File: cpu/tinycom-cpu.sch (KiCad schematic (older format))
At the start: 4 parts, among them P1 CONN_02X08, P2 CONN_02X08, U1 OLIMEX_IC_A13, U2 H5TQG63BFR/FBGA96

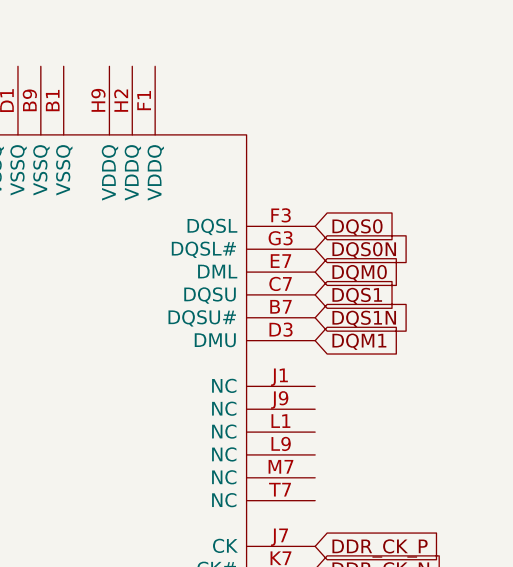
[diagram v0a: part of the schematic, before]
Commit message: add missing ddr connecitons
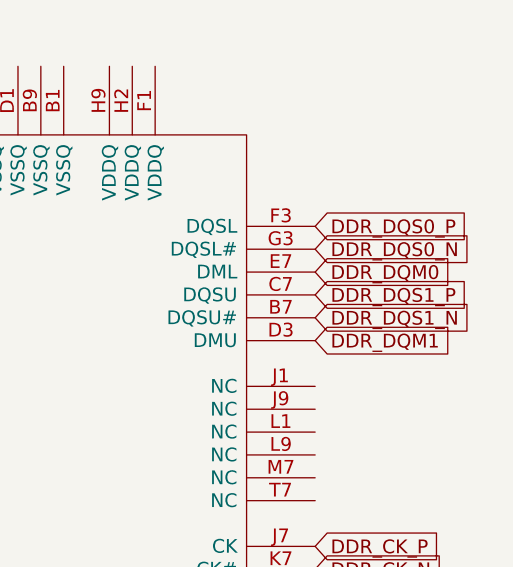
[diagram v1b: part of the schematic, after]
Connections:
- net DQM0 is gone; now on net DDR_DQM0: U2.E7 (DML)
- net DQM1 is gone; now on net DDR_DQM1: U2.D3 (DMU)
- net DQS0 is gone; now on net DDR_DQS0_P: U2.F3 (DQSL)
- net DQS0N is gone; now on net DDR_DQS0_N: U2.G3 (DQSL#)
- net DQS1N is gone; now on net DDR_DQS1_N: U2.B7 (DQSU#)
- net DQS1 renamed DDR_DQS1_P
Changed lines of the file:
@@
 LIBS:sn75lvds83
 LIBS:sy8008baac
-LIBS:cellpilot-cache
+LIBS:tinycom-cpu-cache
 EELAYER 25 0
 EELAYER END
@@
 DDR_CKE
 Text GLabel 10800 -400 2    60   Input ~ 0
-DQS1
+DDR_DQS1_P
 Text GLabel 10800 -300 2    60   Input ~ 0
-DQS1N
+DDR_DQS1_N
 Text GLabel 10800 -700 2    60   Input ~ 0
-DQS0
+DDR_DQS0_P
 Text GLabel 10800 -600 2    60   Input ~ 0
-DQS0N
+DDR_DQS0_N
 Text GLabel 10800 -500 2    60   Input ~ 0
-DQM0
+DDR_DQM0
 Text GLabel 10800 -200 2    60   Input ~ 0
-DQM1
+DDR_DQM1
 Text GLabel 10800 3600 2    60   Input ~ 0
 DDR_ODT

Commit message: add routes
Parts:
- added C1, C2: C_Small, Capacitors_SMD:C_0402, symbol C_Small
- added R? (x3): R, symbol R
- added Y1: Crystal, Crystals:crystal_FA238-TSX3225, symbol Crystal
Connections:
- net +1V5: now reaches U2.A1 (VDDQ)
- net +1V5: now also P1.12 (P12), U1.23 (VCC1_DRAM), U1.30 (VCC2_DRAM), U1.43 (VCC3_DRAM), U1.53 (VCC4_DRAM), U1.62 (VCC5_DRAM), U2.A8 (VDDQ), U2.B2 (VDD), U2.C1 (VDDQ), U2.C9 (VDDQ), U2.D2 (VDDQ), U2.D9 (VDD), U2.E9 (VDDQ), U2.F1 (VDDQ), U2.G7 (VDD), U2.H2 (VDDQ), U2.H9 (VDDQ), U2.K2 (VDD), U2.K8 (VDD), U2.N1 (VDD), U2.N9 (VDD), U2.R1 (VDD), U2.R9 (VDD), R?.1
- net GND: now reaches U2.A9 (VSS)
- net GND: now also P2.10 (P10), P2.12 (P12), P2.14 (P14), P2.16 (P16), U1.159 (RESET_N), U2.B1 (VSSQ), U2.B3 (VSS), U2.B9 (VSSQ), U2.D1 (VSSQ), U2.D8 (VSSQ), U2.E1 (VSS), U2.E2 (VSSQ), U2.E8 (VSSQ), U2.F9 (VSSQ), U2.G1 (VSSQ), U2.G8 (VSS), U2.G9 (VSSQ), U2.J2 (VSS), U2.J8 (VSS), U2.L2 (CS), U2.M1 (VSS), U2.M9 (VSS), U2.P1 (VSS), U2.P9 (VSS), U2.T1 (VSS), U2.T9 (VSS), C1.2, C2.2, R?.2, R?.2
- net at U2.H1 (VREFDQ): now also U2.M8 (VREFCA), R?.1, R?.2
- net at U2.L8 (ZQ): now also R?.1
- net +3V3: now reaches U1.100 (VCC2)
- net +3V3: now also P1.16 (P16), U1.142 (VCC3), U1.163 (VCC4), U1.5 (VCC1), U1.76 (V33_HP), U1.80 (VRP), U1.82 (VRA2), U1.83 (VRA1), U1.97 (V33_USB)
- net SDC0_D1: now reaches U1.107 (PF0/SDC0_D1/JTAG_TMS)
- net SDC0_D1: now also P1.1 (P1)
- net SDC0_D0: now reaches U1.108 (PF1/SDC0_D0/JTAG_TDI)
- net SDC0_D0: now also P1.3 (P3)
- net VCC_14: now reaches U1.109 (VDD4_INT)
- net VCC_14: now also P1.10 (P10), U1.11 (VDD3_CPU), U1.149 (VDD5_INT), U1.156 (VDD5_CPU), U1.16 (VDD4_CPU), U1.164 (VDD6_CPU), U1.169 (VDD7_CPU), U1.173 (VDD8_CPU), U1.35 (VDD1_INT), U1.4 (VDD1_CPU), U1.73 (VDD2_INT), U1.9 (VDD2_CPU), U1.98 (VDD3-INT)
- net SDC0_CLK: now reaches U1.110 (PF2/SDC0_CLK/UART0_TX)
- net SDC0_CLK: now also P1.5 (P5)
- net SDC0_CMD: now reaches U1.111 (PF3/SDC0_CMD/JTAG_TDO)
- net SDC0_CMD: now also P1.7 (P7)
- net SDC0_D3: now reaches U1.112 (PF4/SDC0_D3/UART0_RX)
- net SDC0_D3: now also P1.9 (P9)
- net SDC0_D2: now reaches U1.113 (PF5/SDC0_D2/JTAG_TCK)
- net SDC0_D2: now also P1.11 (P11)
- net CSI_CLK: now reaches U1.114 (PE0/CSI_PCLK/SPI2_CS0/EINT14)
- net CSI_CLK: now also P2.1 (P1)
- net CSI_MCLK: now reaches U1.115 (PE1/CSI_MCLK/SPI2_CLK/EINT15)
- net CSI_MCLK: now also P2.3 (P3)
- net CSI_HSYNC: now reaches U1.116 (PE2/CSI_HSYNC/SPI2_MOSI)
- net CSI_HSYNC: now also P2.5 (P5)
- net CSI_VSYNC: now reaches U1.117 (PE3/CSI_VSYNC/SPI2_MISO)
- net CSI_VSYNC: now also P2.7 (P7)
- net CSI_D0: now reaches U1.118 (PE4/CSI_D0/SDC2_D0)
- net CSI_D0: now also P2.9 (P9)
- net CSI_D1: now reaches U1.119 (PE5/CSI_D1/SDC2_D1)
- net CSI_D1: now also P2.11 (P11)
- net CSI_D2: now reaches U1.120 (PE6/CSI_D2/SDC2_D2)
- net CSI_D2: now also P2.13 (P13)
- net CSI_D3: now reaches U1.121 (PE7/CSI_D3/SDC2_D3)
- net CSI_D3: now also P2.15 (P15)
- net CSI_D4: now reaches U1.122 (PE8/CSI_D4/SDC2_CMD)
- net CSI_D4: now also P2.2 (P2)
- net CSI_D5: now reaches U1.123 (PE9/CSI_D5/SDC2_CLK)
- net CSI_D5: now also P2.4 (P4)
- net CSI_D6: now reaches U1.124 (PE10/CSI_D6/UART1_TX)
- net CSI_D6: now also P2.6 (P6)
- net CSI_D7: now reaches U1.125 (PE11/CSI_D7/UART1_RX)
- net CSI_D7: now also P2.8 (P8)
- net UART1_RX: now reaches U1.151 (PG4/UART1_RX/EINT4)
- net UART1_RX: now also P1.15 (P15)
- net UART1_TX: now reaches U1.152 (PG3/UART1_TX/EINT3)
- net UART1_TX: now also P1.13 (P13)
- net at U1.79 (AGND): now also U1.GND_ (GND)
- net VCC_30: now reaches U1.81 (AVCC)
- net VCC_30: now also P1.14 (P14)
- net at U1.91 (X24MOUT): now also C2.1, Y1.2
- net at U1.92 (X24MIN): now also C1.1, Y1.1
- net UDM0: now reaches U1.93 (UDM0)
- net UDM0: now also P1.2 (P2)
- net UDP0: now reaches U1.94 (UDP0)
- net UDP0: now also P1.4 (P4)
- net UDM1: now reaches U1.95 (UDM1)
- net UDM1: now also P1.6 (P6)
- net UDP1: now reaches U1.96 (UDP1)
- net UDP1: now also P1.8 (P8)
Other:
- moved on the sheet: P2

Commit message: add routes
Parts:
- C1, C2: footprint Capacitors_SMD:C_0402 -> Capacitors_SMD:C_0603
- R1, R2, R3: renamed from R?; footprint (none) -> Resistors_SMD:R_0603
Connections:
- net GND: no longer P2.10 (P10)
- net MICIN1: now reaches U1.84 (MICIN1)
- net MICIN1: now also P2.10 (P10)
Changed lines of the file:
@@
 GND
 Text GLabel 9400 5800 2    60   Input ~ 0
-GND
+MICIN1
 Text GLabel 1550 -1650 0    60   Input ~ 0
 VCC_33
@@
 F 0 "C1" H 810 1920 50  0000 L CNN
 F 1 "C_Small" H 810 1770 50  0000 L CNN
-F 2 "Capacitors_SMD:C_0402" H 800 1850 60  0001 C CNN
+F 2 "Capacitors_SMD:C_0603" H 800 1850 60  0001 C CNN
 F 3 "" H 800 1850 60  0000 C CNN
 	1    800  1850
@@
 F 0 "C2" H 810 2220 50  0000 L CNN
 F 1 "C_Small" H 810 2070 50  0000 L CNN
-F 2 "Capacitors_SMD:C_0402" H 800 2150 60  0001 C CNN
+F 2 "Capacitors_SMD:C_0603" H 800 2150 60  0001 C CNN
 F 3 "" H 800 2150 60  0000 C CNN
 	1    800  2150
@@
 $EndComp
 $Comp
-L GND #PWR?
+L GND #PWR06
 U 1 1 5624D2FA
 P 8100 2900
-F 0 "#PWR?" H 8100 2650 50  0001 C CNN
+F 0 "#PWR06" H 8100 2650 50  0001 C CNN
 F 1 "GND" H 8100 2750 50  0000 C CNN
 F 2 "" H 8100 2900 60  0000 C CNN
@@
 $EndComp
 $Comp
-L GND #PWR?
+L GND #PWR07
 U 1 1 5624DA0C
 P 8750 -1400
-F 0 "#PWR?" H 8750 -1650 50  0001 C CNN
+F 0 "#PWR07" H 8750 -1650 50  0001 C CNN
 F 1 "GND" H 8750 -1550 50  0000 C CNN
 F 2 "" H 8750 -1400 60  0000 C CNN
@@
 $EndComp
 $Comp
-L +1V5 #PWR?
+L +1V5 #PWR08
 U 1 1 5624DE1D
 P 10200 -1600
-F 0 "#PWR?" H 10200 -1750 50  0001 C CNN
+F 0 "#PWR08" H 10200 -1750 50  0001 C CNN
 F 1 "+1V5" H 10200 -1460 50  0000 C CNN
 F 2 "" H 10200 -1600 60  0000 C CNN
@@
 $EndComp
 $Comp
-L +1V5 #PWR?
+L +1V5 #PWR09
 U 1 1 5624E0CB
 P 8100 -650
-F 0 "#PWR?" H 8100 -800 50  0001 C CNN
+F 0 "#PWR09" H 8100 -800 50  0001 C CNN
 F 1 "+1V5" H 8100 -510 50  0000 C CNN
 F 2 "" H 8100 -650 60  0000 C CNN
@@
 $EndComp
 $Comp
-L +1V5 #PWR?
+L +1V5 #PWR010
 U 1 1 5624EEEC
 P 8600 4500
-F 0 "#PWR?" H 8600 4350 50  0001 C CNN
+F 0 "#PWR010" H 8600 4350 50  0001 C CNN
 F 1 "+1V5" H 8600 4640 50  0000 C CNN
 F 2 "" H 8600 4500 60  0000 C CNN
@@
 $EndComp
 $Comp
-L +1V5 #PWR?
+L +1V5 #PWR011
 U 1 1 5624F29C
 P 7450 3050
-F 0 "#PWR?" H 7450 2900 50  0001 C CNN
+F 0 "#PWR011" H 7450 2900 50  0001 C CNN
 F 1 "+1V5" H 7450 3190 50  0000 C CNN
 F 2 "" H 7450 3050 60  0000 C CNN
@@
 $EndComp
 $Comp
-L R R?
+L R R1
 U 1 1 5624F4CA
 P 7450 3300
-F 0 "R?" V 7530 3300 50  0000 C CNN
+F 0 "R1" V 7530 3300 50  0000 C CNN
 F 1 "R" V 7450 3300 50  0000 C CNN
-F 2 "" V 7380 3300 30  0000 C CNN
+F 2 "Resistors_SMD:R_0603" V 7380 3300 30  0001 C CNN
 F 3 "" H 7450 3300 30  0000 C CNN
 	1    7450 3300
@@
 $EndComp
 $Comp
-L R R?
+L R R2
 U 1 1 5624F53F
 P 7450 3800
-F 0 "R?" V 7530 3800 50  0000 C CNN
+F 0 "R2" V 7530 3800 50  0000 C CNN
 F 1 "R" V 7450 3800 50  0000 C CNN
-F 2 "" V 7380 3800 30  0000 C CNN
+F 2 "Resistors_SMD:R_0603" V 7380 3800 30  0001 C CNN
 F 3 "" H 7450 3800 30  0000 C CNN
 	1    7450 3800
@@
 $EndComp
 $Comp
-L GND #PWR?
+L GND #PWR012
 U 1 1 5624F924
 P 7450 4150
-F 0 "#PWR?" H 7450 3900 50  0001 C CNN
+F 0 "#PWR012" H 7450 3900 50  0001 C CNN
 F 1 "GND" H 7450 4000 50  0000 C CNN
 F 2 "" H 7450 4150 60  0000 C CNN
@@
 $EndComp
 $Comp
-L GND #PWR?
+L GND #PWR013
 U 1 1 562500B4
 P 11450 3550
-F 0 "#PWR?" H 11450 3300 50  0001 C CNN
+F 0 "#PWR013" H 11450 3300 50  0001 C CNN
 F 1 "GND" H 11450 3400 50  0000 C CNN
 F 2 "" H 11450 3550 60  0000 C CNN
@@
 $EndComp
 $Comp
-L R R?
+L R R3
 U 1 1 56250400
 P 11450 4000
-F 0 "R?" V 11530 4000 50  0000 C CNN
+F 0 "R3" V 11530 4000 50  0000 C CNN
 F 1 "R" V 11450 4000 50  0000 C CNN
-F 2 "" V 11380 4000 30  0000 C CNN
+F 2 "Resistors_SMD:R_0603" V 11380 4000 30  0001 C CNN
 F 3 "" H 11450 4000 30  0000 C CNN
 	1    11450 4000
@@
 	11450 3800 11450 3850
 $Comp
-L GND #PWR?
+L GND #PWR014
 U 1 1 562507C8
 P 11450 4300
-F 0 "#PWR?" H 11450 4050 50  0001 C CNN
+F 0 "#PWR014" H 11450 4050 50  0001 C CNN
 F 1 "GND" H 11450 4150 50  0000 C CNN
 F 2 "" H 11450 4300 60  0000 C CNN
@@
 Wire Wire Line
 	11450 4150 11450 4300
+Text GLabel 1650 4200 0    60   Input ~ 0
+MICIN1
 $EndSCHEMATC

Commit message: full ddr route
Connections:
- net GND: now also U2.J9 (NC)
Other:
- note added: "for routing..."
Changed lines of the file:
@@
 Text GLabel 1650 4200 0    60   Input ~ 0
 MICIN1
+$Comp
+L GND #PWR?
+U 1 1 56250BEE
+P 11000 150
+F 0 "#PWR?" H 11000 -100 50  0001 C CNN
+F 1 "GND" H 11000 0   50  0000 C CNN
+F 2 "" H 11000 150 60  0000 C CNN
+F 3 "" H 11000 150 60  0000 C CNN
+	1    11000 150
+	1    0    0    -1
+$EndComp
+Wire Wire Line
+	10800 100  11000 100
+Wire Wire Line
+	11000 100  11000 150
+Text Notes 11050 100  0    60   ~ 0
+for routing...
 $EndSCHEMATC

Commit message: fix ddr routing
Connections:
- net DDR_QDS1_P is gone; now on net DDR_DQS1_P: U1.33 (DDR3_DQS1)
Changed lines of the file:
@@
 DDR_DQS0_N
 Text GLabel 5050 3200 2    60   Input ~ 0
-DDR_QDS1_P
+DDR_DQS1_P
 Text GLabel 5050 3300 2    60   Input ~ 0
 DDR_DQS1_N
@@
 MICIN1
 $Comp
-L GND #PWR?
+L GND #PWR015
 U 1 1 56250BEE
 P 11000 150
-F 0 "#PWR?" H 11000 -100 50  0001 C CNN
+F 0 "#PWR015" H 11000 -100 50  0001 C CNN
 F 1 "GND" H 11000 0   50  0000 C CNN
 F 2 "" H 11000 150 60  0000 C CNN

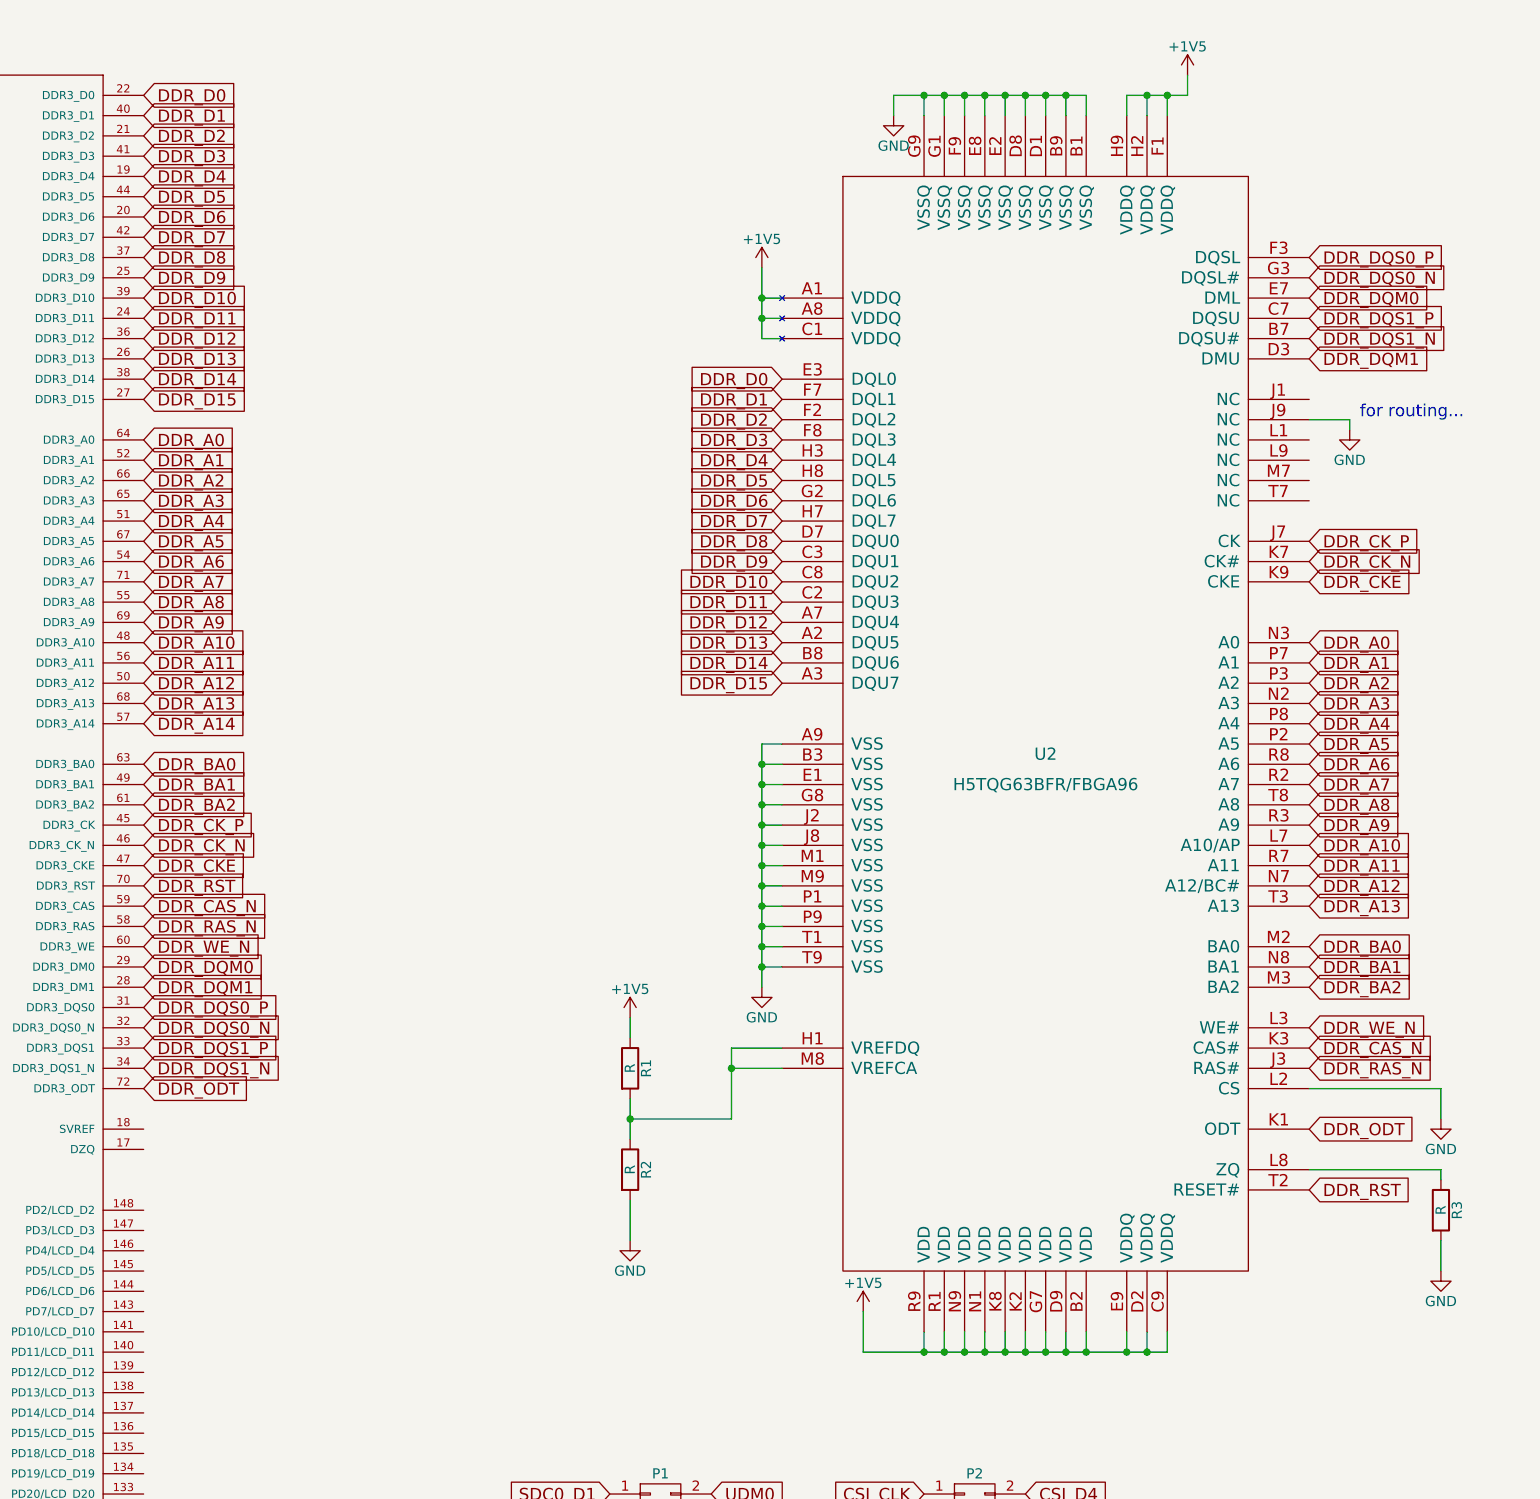
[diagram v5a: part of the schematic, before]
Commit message: change ddr to bga78
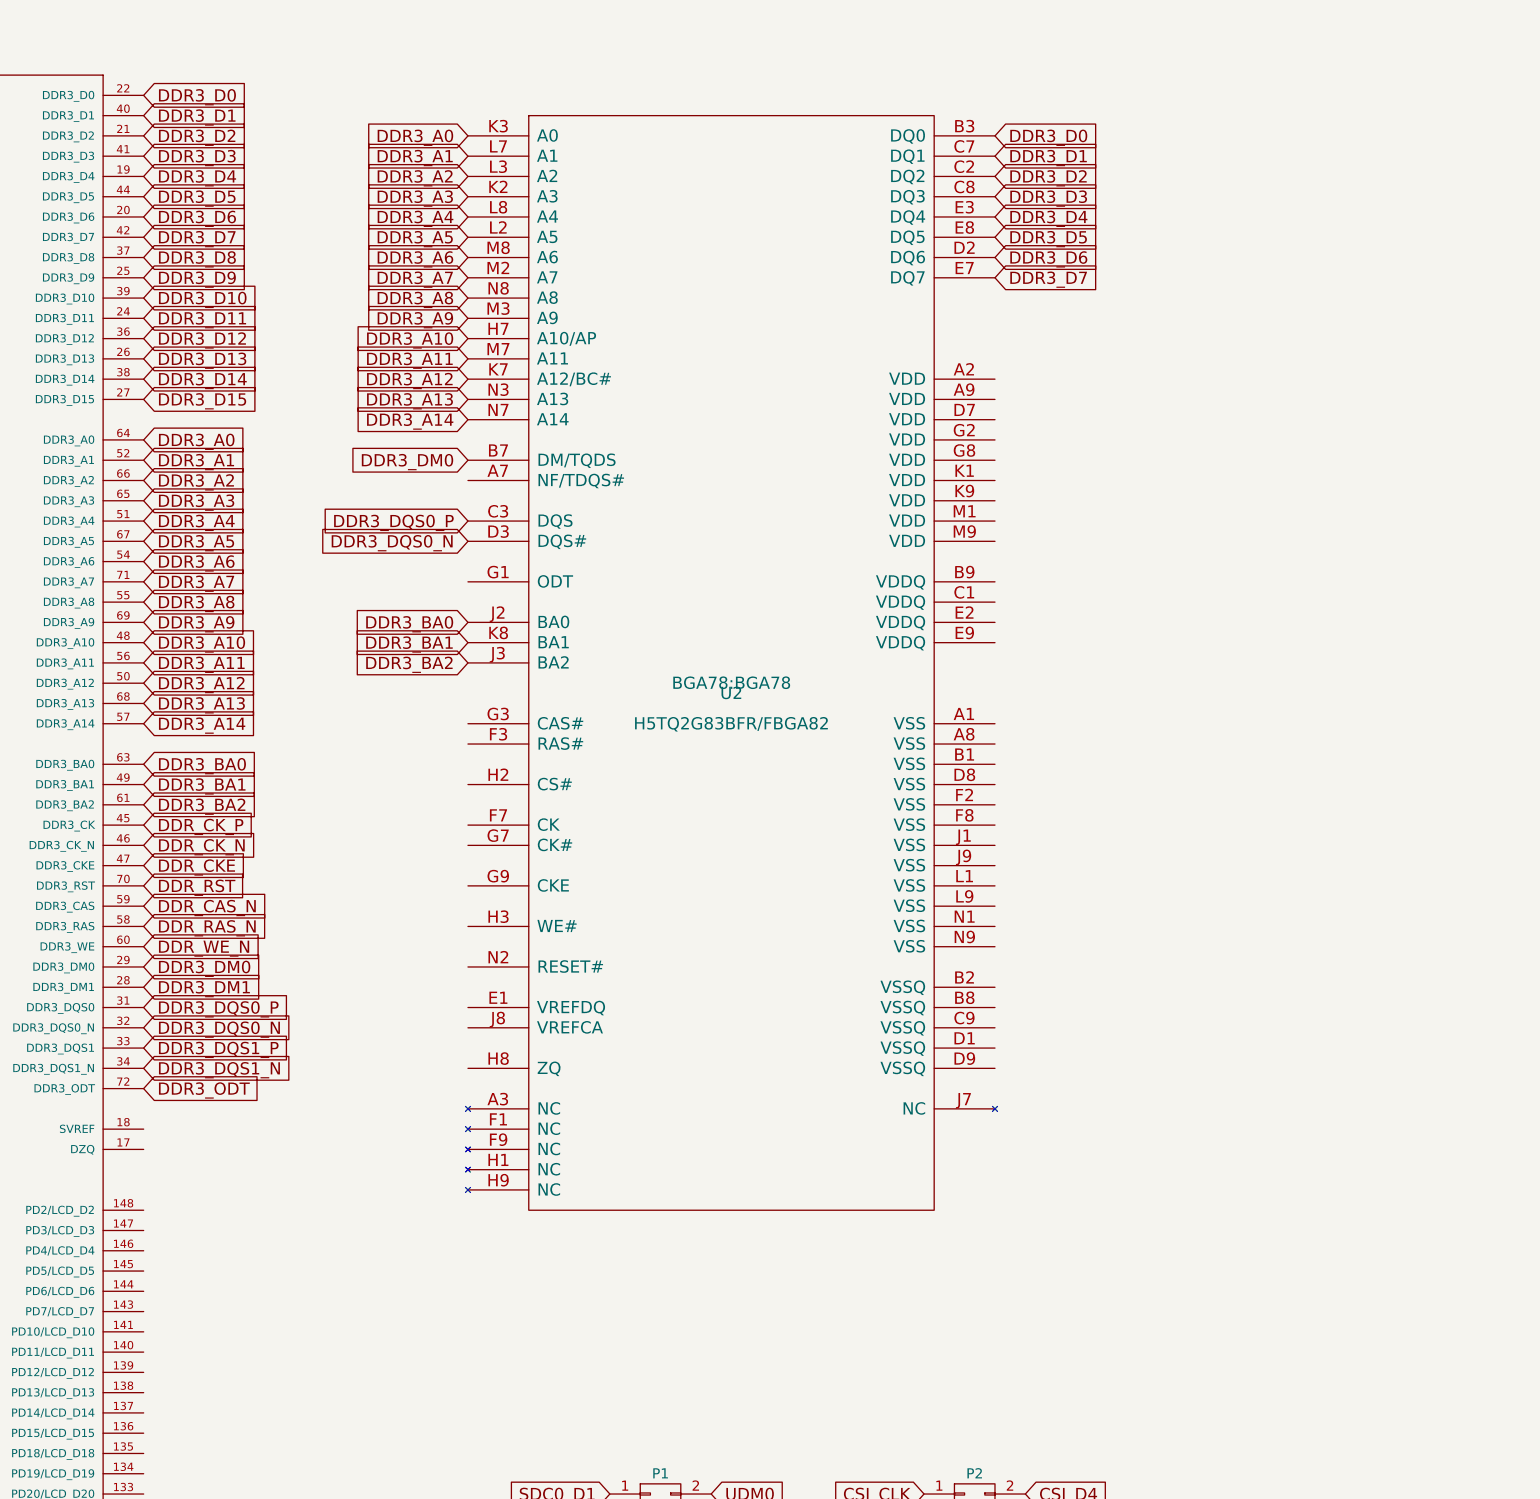
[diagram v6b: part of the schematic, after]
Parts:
- removed R1, R2, R3: R, Resistors_SMD:R_0603, symbol R
- removed U2: H5TQG63BFR/FBGA96, ax209:ax209-OLIMEX_IC_FBGA96, symbol H5TQG63BFR/FBGA96
- added U2: H5TQ2G83BFR/FBGA82, BGA78:BGA78, symbol H5TQ2G83BFR/FBGA82
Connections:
- net DDR_A0 renamed DDR3_A0
- net DDR3_A0: now also U2.K3 (A0)
- net DDR_A1 renamed DDR3_A1
- net DDR3_A1: now also U2.L7 (A1)
- net DDR_A10 renamed DDR3_A10
- net DDR3_A10: now also U2.H7 (A10/AP)
- net DDR_A11 renamed DDR3_A11
- net DDR3_A11: now also U2.M7 (A11)
- net DDR_A12 renamed DDR3_A12
- net DDR3_A12: now also U2.K7 (A12/BC#)
- net DDR_A13 renamed DDR3_A13
- net DDR3_A13: now also U2.N3 (A13)
- net DDR_A14 renamed DDR3_A14
- net DDR3_A14: now also U2.N7 (A14)
- net DDR_A2 renamed DDR3_A2
- net DDR3_A2: now also U2.L3 (A2)
- net DDR_A3 renamed DDR3_A3
- net DDR3_A3: now also U2.K2 (A3)
- net DDR_A4 renamed DDR3_A4
- net DDR3_A4: now also U2.L8 (A4)
- net DDR_A5 renamed DDR3_A5
- net DDR3_A5: now also U2.L2 (A5)
- net DDR_A6 renamed DDR3_A6
- net DDR3_A6: now also U2.M8 (A6)
- net DDR_A7 renamed DDR3_A7
- net DDR3_A7: now also U2.M2 (A7)
- net DDR_A8 renamed DDR3_A8
- net DDR3_A8: now also U2.N8 (A8)
- net DDR_A9 renamed DDR3_A9
- net DDR3_A9: now also U2.M3 (A9)
- net DDR_BA0 renamed DDR3_BA0
- net DDR3_BA0: now also U2.J2 (BA0)
- net DDR_BA1 renamed DDR3_BA1
- net DDR3_BA1: now also U2.K8 (BA1)
- net DDR_BA2 renamed DDR3_BA2
- net DDR3_BA2: now also U2.J3 (BA2)
- net DDR_D0 renamed DDR3_D0
- net DDR3_D0: now also U2.B3 (DQ0)
- net DDR_D1 renamed DDR3_D1
- net DDR3_D1: now also U2.C7 (DQ1)
- net DDR_D10 renamed DDR3_D10
- net DDR_D11 renamed DDR3_D11
- net DDR_D12 renamed DDR3_D12
- net DDR_D13 renamed DDR3_D13
- net DDR_D14 renamed DDR3_D14
- net DDR_D15 renamed DDR3_D15
- net DDR_D2 renamed DDR3_D2
- net DDR3_D2: now also U2.C2 (DQ2)
- net DDR_D3 renamed DDR3_D3
- net DDR3_D3: now also U2.C8 (DQ3)
- net DDR_D4 renamed DDR3_D4
- net DDR3_D4: now also U2.E3 (DQ4)
- net DDR_D5 renamed DDR3_D5
- net DDR3_D5: now also U2.E8 (DQ5)
- net DDR_D6 renamed DDR3_D6
- net DDR3_D6: now also U2.D2 (DQ6)
- net DDR_D7 renamed DDR3_D7
- net DDR3_D7: now also U2.E7 (DQ7)
- net DDR_D8 renamed DDR3_D8
- net DDR_D9 renamed DDR3_D9
- net DDR_DQM0 renamed DDR3_DM0
- net DDR3_DM0: now also U2.B7 (DM/TQDS)
- net DDR_DQM1 renamed DDR3_DM1
- net DDR_DQS0_N renamed DDR3_DQS0_N
- net DDR3_DQS0_N: now also U2.D3 (DQS#)
- net DDR_DQS0_P renamed DDR3_DQS0_P
- net DDR3_DQS0_P: now also U2.C3 (DQS)
- net DDR_DQS1_N renamed DDR3_DQS1_N
- net DDR_DQS1_P renamed DDR3_DQS1_P
- net DDR_ODT renamed DDR3_ODT
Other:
- note removed: "for routing..."
